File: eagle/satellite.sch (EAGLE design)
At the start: 10 parts

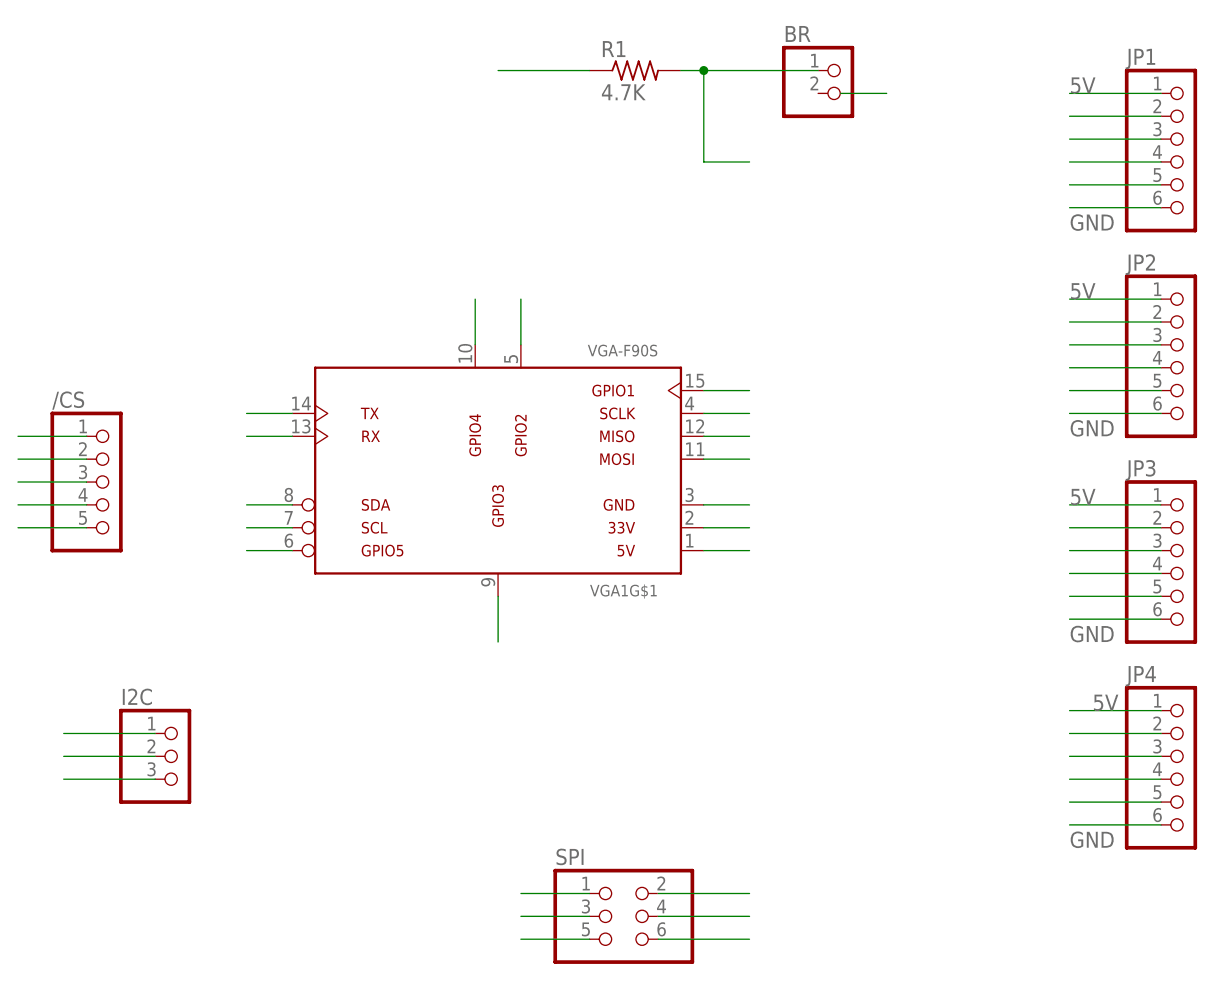
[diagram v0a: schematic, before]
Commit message: modified satellite board to fix incorrect routing
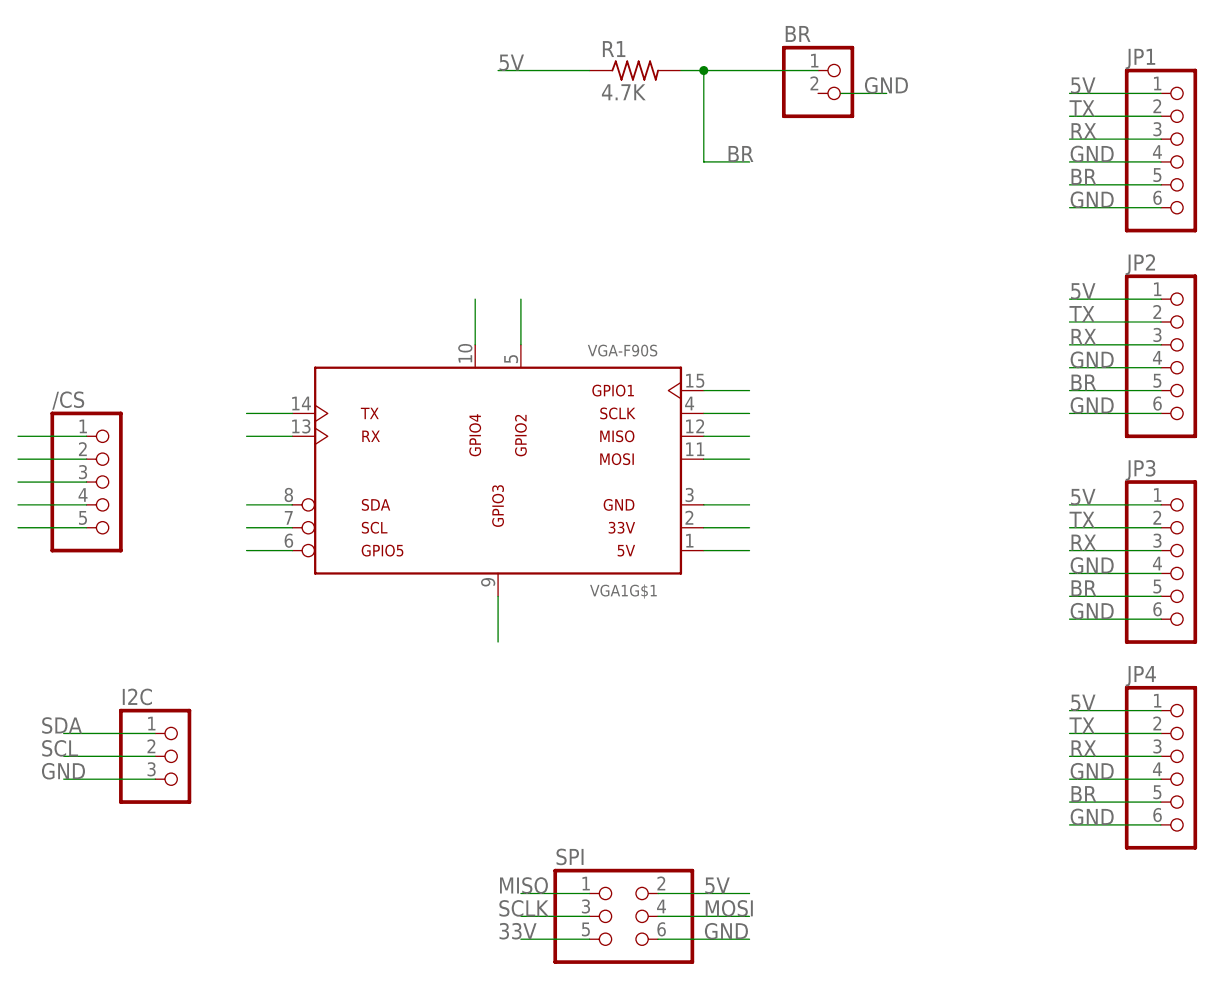
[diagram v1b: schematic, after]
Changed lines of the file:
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@@
 <pinref part="JP1" gate="A" pin="2"/>
 <wire x1="147.32" y1="101.6" x2="137.16" y2="101.6" width="0.1524" layer="91"/>
+<label x="137.16" y="101.6" size="1.778" layer="95"/>
 </segment>
 <segment>
 <pinref part="JP4" gate="A" pin="2"/>
 <wire x1="147.32" y1="33.02" x2="137.16" y2="33.02" width="0.1524" layer="91"/>
+<label x="137.16" y="33.02" size="1.778" layer="95"/>
 </segment>
 <segment>
 <pinref part="JP3" gate="A" pin="2"/>
 <wire x1="147.32" y1="55.88" x2="137.16" y2="55.88" width="0.1524" layer="91"/>
+<label x="137.16" y="55.88" size="1.778" layer="95"/>
 </segment>
 <segment>
 <pinref part="JP2" gate="A" pin="2"/>
 <wire x1="147.32" y1="78.74" x2="137.16" y2="78.74" width="0.1524" layer="91"/>
+<label x="137.16" y="78.74" size="1.778" layer="95"/>
 </segment>
 <segment>
@@
 <pinref part="SPI" gate="A" pin="3"/>
 <wire x1="76.2" y1="12.7" x2="83.82" y2="12.7" width="0.1524" layer="91"/>
+<label x="73.66" y="12.7" size="1.778" layer="95"/>
 </segment>
 </net>
@@
 <pinref part="JP1" gate="A" pin="5"/>
 <wire x1="147.32" y1="93.98" x2="137.16" y2="93.98" width="0.1524" layer="91"/>
+<label x="137.16" y="93.98" size="1.778" layer="95"/>
 </segment>
 <segment>
 <pinref part="JP2" gate="A" pin="5"/>
 <wire x1="147.32" y1="71.12" x2="137.16" y2="71.12" width="0.1524" layer="91"/>
+<label x="137.16" y="71.12" size="1.778" layer="95"/>
 </segment>
 <segment>
 <pinref part="JP3" gate="A" pin="5"/>
 <wire x1="147.32" y1="48.26" x2="137.16" y2="48.26" width="0.1524" layer="91"/>
+<label x="137.16" y="48.26" size="1.778" layer="95"/>
 </segment>
 <segment>
 <pinref part="JP4" gate="A" pin="5"/>
 <wire x1="137.16" y1="25.4" x2="147.32" y2="25.4" width="0.1524" layer="91"/>
+<label x="137.16" y="25.4" size="1.778" layer="95"/>
 </segment>
 <segment>
@@
 <junction x="96.52" y="106.68"/>
 <wire x1="96.52" y1="96.52" x2="101.6" y2="96.52" width="0.1524" layer="91"/>
+<label x="99.06" y="96.52" size="1.778" layer="95"/>
 </segment>
 </net>
@@
 <pinref part="JP4" gate="A" pin="1"/>
 <wire x1="147.32" y1="35.56" x2="137.16" y2="35.56" width="0.1524" layer="91"/>
-<label x="139.7" y="35.56" size="1.778" layer="95"/>
+<label x="137.16" y="35.56" size="1.778" layer="95"/>
 </segment>
 <segment>
@@
 <pinref part="R1" gate="G$1" pin="1"/>
 <wire x1="73.66" y1="106.68" x2="83.82" y2="106.68" width="0.1524" layer="91"/>
+<label x="73.66" y="106.68" size="1.778" layer="95"/>
 </segment>
 <segment>
 <pinref part="SPI" gate="A" pin="2"/>
 <wire x1="101.6" y1="15.24" x2="91.44" y2="15.24" width="0.1524" layer="91"/>
+<label x="96.52" y="15.24" size="1.778" layer="95"/>
 </segment>
 </net>
@@
 <pinref part="JP1" gate="A" pin="3"/>
 <wire x1="147.32" y1="99.06" x2="137.16" y2="99.06" width="0.1524" layer="91"/>
+<label x="137.16" y="99.06" size="1.778" layer="95"/>
 </segment>
 <segment>
@@
 <pinref part="JP2" gate="A" pin="3"/>
 <wire x1="147.32" y1="76.2" x2="137.16" y2="76.2" width="0.1524" layer="91"/>
+<label x="137.16" y="76.2" size="1.778" layer="95"/>
 </segment>
 <segment>
 <pinref part="JP3" gate="A" pin="3"/>
 <wire x1="147.32" y1="53.34" x2="137.16" y2="53.34" width="0.1524" layer="91"/>
+<label x="137.16" y="53.34" size="1.778" layer="95"/>
 </segment>
 <segment>
 <pinref part="JP4" gate="A" pin="3"/>
 <wire x1="137.16" y1="30.48" x2="147.32" y2="30.48" width="0.1524" layer="91"/>
+<label x="137.16" y="30.48" size="1.778" layer="95"/>
 </segment>
 </net>
@@
 <pinref part="SPI" gate="A" pin="1"/>
 <wire x1="83.82" y1="15.24" x2="76.2" y2="15.24" width="0.1524" layer="91"/>
+<label x="73.66" y="15.24" size="1.778" layer="95"/>
 </segment>
 </net>
@@
 <pinref part="I2C" gate="A" pin="1"/>
 <wire x1="35.56" y1="33.02" x2="25.4" y2="33.02" width="0.1524" layer="91"/>
+<label x="22.86" y="33.02" size="1.778" layer="95"/>
 </segment>
 </net>
@@
 <pinref part="I2C" gate="A" pin="2"/>
 <wire x1="35.56" y1="30.48" x2="25.4" y2="30.48" width="0.1524" layer="91"/>
+<label x="22.86" y="30.48" size="1.778" layer="95"/>
 </segment>
 </net>
@@
 <pinref part="SPI" gate="A" pin="4"/>
 <wire x1="91.44" y1="12.7" x2="101.6" y2="12.7" width="0.1524" layer="91"/>
+<label x="96.52" y="12.7" size="1.778" layer="95"/>
 </segment>
 </net>
@@
 <pinref part="JP1" gate="A" pin="6"/>
 <wire x1="137.16" y1="91.44" x2="147.32" y2="91.44" width="0.1524" layer="91"/>
-<label x="137.16" y="88.9" size="1.778" layer="95"/>
+<label x="137.16" y="91.44" size="1.778" layer="95"/>
 </segment>
 <segment>
 <pinref part="JP2" gate="A" pin="6"/>
 <wire x1="147.32" y1="68.58" x2="137.16" y2="68.58" width="0.1524" layer="91"/>
-<label x="137.16" y="66.04" size="1.778" layer="95"/>
+<label x="137.16" y="68.58" size="1.778" layer="95"/>
 </segment>
 <segment>
 <pinref part="JP3" gate="A" pin="6"/>
 <wire x1="147.32" y1="45.72" x2="137.16" y2="45.72" width="0.1524" layer="91"/>
-<label x="137.16" y="43.18" size="1.778" layer="95"/>
+<label x="137.16" y="45.72" size="1.778" layer="95"/>
 </segment>
 <segment>
 <pinref part="JP4" gate="A" pin="6"/>
 <wire x1="137.16" y1="22.86" x2="147.32" y2="22.86" width="0.1524" layer="91"/>
-<label x="137.16" y="20.32" size="1.778" layer="95"/>
+<label x="137.16" y="22.86" size="1.778" layer="95"/>
 </segment>
 <segment>
 <pinref part="JP1" gate="A" pin="4"/>
 <wire x1="147.32" y1="96.52" x2="137.16" y2="96.52" width="0.1524" layer="91"/>
+<label x="137.16" y="96.52" size="1.778" layer="95"/>
 </segment>
 <segment>
 <pinref part="JP2" gate="A" pin="4"/>
 <wire x1="147.32" y1="73.66" x2="137.16" y2="73.66" width="0.1524" layer="91"/>
+<label x="137.16" y="73.66" size="1.778" layer="95"/>
 </segment>
 <segment>
 <pinref part="JP3" gate="A" pin="4"/>
 <wire x1="147.32" y1="50.8" x2="137.16" y2="50.8" width="0.1524" layer="91"/>
+<label x="137.16" y="50.8" size="1.778" layer="95"/>
 </segment>
 <segment>
 <pinref part="JP4" gate="A" pin="4"/>
 <wire x1="137.16" y1="27.94" x2="147.32" y2="27.94" width="0.1524" layer="91"/>
+<label x="137.16" y="27.94" size="1.778" layer="95"/>
 </segment>
 <segment>
 <wire x1="111.76" y1="104.14" x2="116.84" y2="104.14" width="0.1524" layer="91"/>
+<label x="114.3" y="104.14" size="1.778" layer="95"/>
 </segment>
 <segment>
 <pinref part="SPI" gate="A" pin="6"/>
 <wire x1="101.6" y1="10.16" x2="91.44" y2="10.16" width="0.1524" layer="91"/>
+<label x="96.52" y="10.16" size="1.778" layer="95"/>
 </segment>
 <segment>
 <pinref part="I2C" gate="A" pin="3"/>
 <wire x1="35.56" y1="27.94" x2="25.4" y2="27.94" width="0.1524" layer="91"/>
+<label x="22.86" y="27.94" size="1.778" layer="95"/>
 </segment>
 </net>
@@
 <pinref part="SPI" gate="A" pin="5"/>
 <wire x1="76.2" y1="10.16" x2="83.82" y2="10.16" width="0.1524" layer="91"/>
-</segment>
-</net>
+<label x="73.66" y="10.16" size="1.778" layer="95"/>
+</segment>
+</net>
